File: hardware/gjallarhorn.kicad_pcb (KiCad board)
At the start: 2 copper layers, 18 parts, among them J1 Conn_01x02, J2 Conn_02x03_Counter_Clockwise, J3 Conn_01x02, J4 Conn_01x03, Q1 Q_NMOS_GDS, SW1 SW_Push, U1 ATTINY2313-20PU, U2 BOOST_REGULATOR, U3 AP1117-33, U4 HC-05_breakout

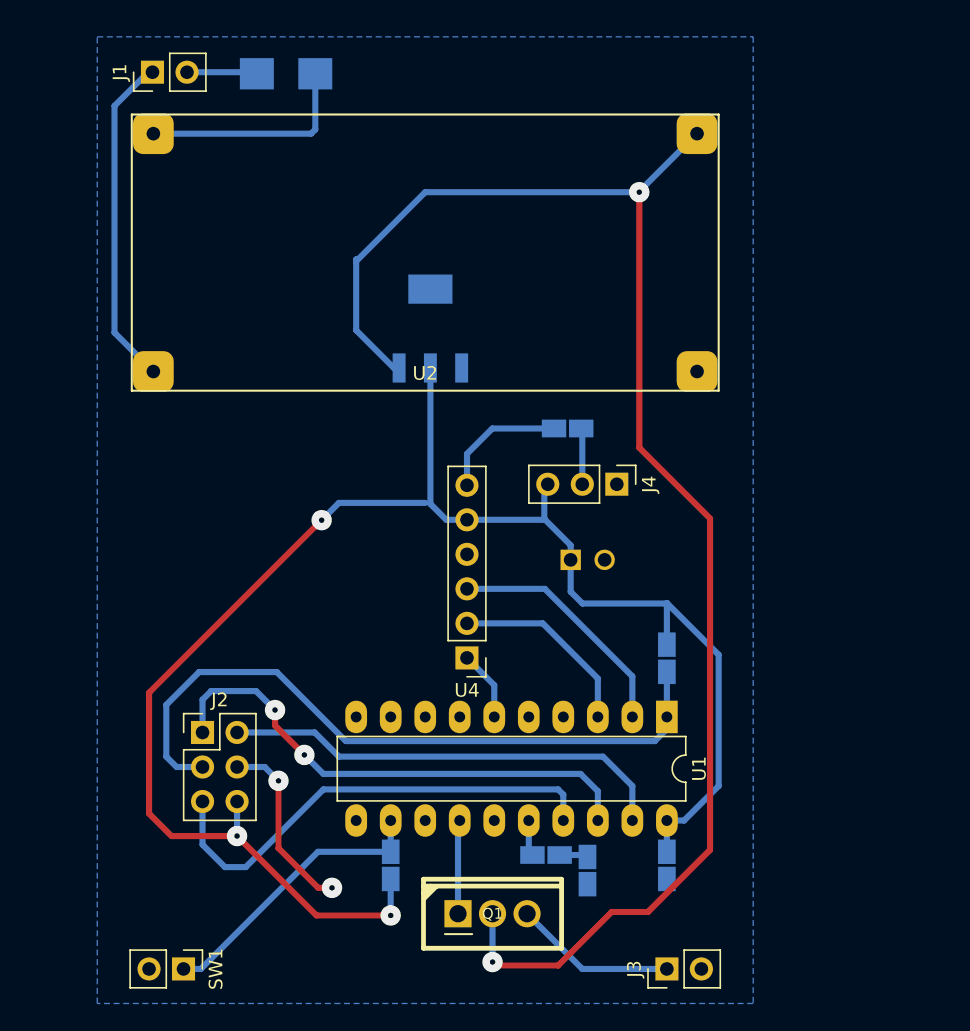
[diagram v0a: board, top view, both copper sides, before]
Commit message: It would be better if I could fit this in a 60x60 square; let's try (in progress).
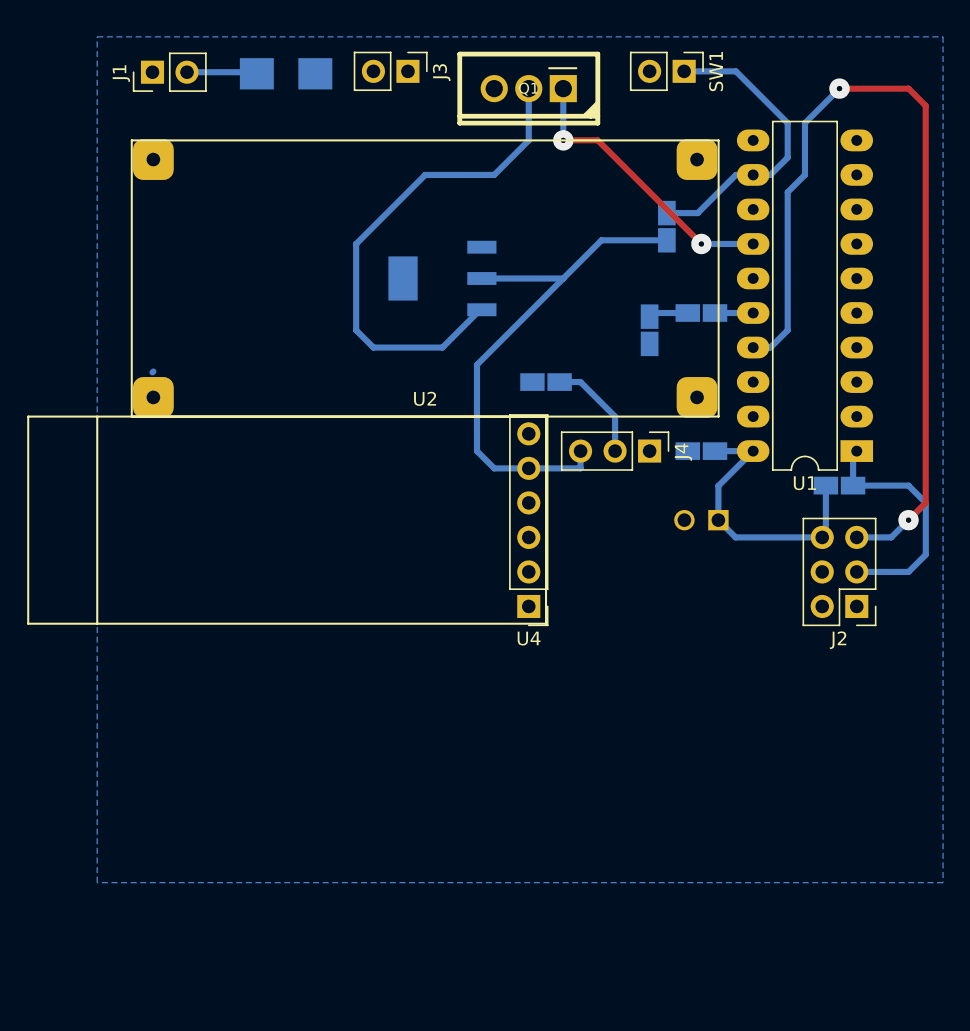
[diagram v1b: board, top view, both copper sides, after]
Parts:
- moved SW1 75.6 mm to (167.6, 38.1)
- moved J3 68.7 mm to (147.3, 38.1), turned to 270 degrees
- moved Q1 60.8 mm to (156.2, 39.4), turned to 180 degrees
- moved R3 51.2 mm to (166.4, 49.5)
- moved J2 49.0 mm to (180.3, 77.5), turned to 180 degrees
- moved R2 41.5 mm to (168.9, 55.9), turned to 180 degrees
- moved D1 40.0 mm to (165.1, 57.1)
- moved C1 30.6 mm to (168.9, 66.0), turned to 0 degrees
- moved U1 24.0 mm to (180.3, 66.0), turned to 180 degrees
- moved R1 18.0 mm to (179.1, 68.6), turned to 180 degrees
- moved C2 8.86 mm to (168.9, 71.1), turned to 270 degrees
- moved U4 5.92 mm to (156.2, 77.5)
- moved U3 3.79 mm to (149.9, 53.3), turned to 270 degrees
- moved R4 3.77 mm to (157.5, 61.0)
- moved J4 3.43 mm to (165.1, 66.0)
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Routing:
- net +12V: track 112.5 -> 36.9 mm, vias 2 -> 0
- net +3V3: track 121.5 -> 60.6 mm, vias 3 -> 0
- net Net-(J2-Pad1): track 37.6 -> 0.00 mm, vias 2 -> 0
- net Net-(J2-Pad3): track 51.3 -> 17.9 mm
- net Net-(J2-Pad2): track 33.3 -> 0.00 mm
- net Net-(J2-Pad5): track 34.8 -> 64.6 mm, vias 0 -> 2
- net Net-(J1-Pad1): track 24.6 -> 0.41 mm
- net Net-(U1-Pad2): track 17.8 -> 0.00 mm
- net Net-(D2-Pad1): track 16.1 -> 0.00 mm
- net Net-(U1-Pad3): track 14.1 -> 0.00 mm
- net GND: track 13.6 -> 0.00 mm, vias 2 -> 0
- net Net-(Q1-Pad1): track 7.80 -> 20.9 mm, vias 0 -> 2
- net Net-(J3-Pad1): track 12.0 -> 0.00 mm
- net Net-(R4-Pad2): track 9.49 -> 0.00 mm
- net Net-(U1-Pad6): track 5.17 -> 0.00 mm
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
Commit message: Moving everything everywhere.
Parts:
- removed J4: Conn_01x03, KiCad/Pin_Headers.pretty:Pin_Header_Straight_1x03_Pitch2.54mm
- added R5: 10k, coddingtonbear/coddingtonbear.pretty:0805_Milling, B.Cu at (139.7, 69.2)
- added R6: 6.8k, coddingtonbear/coddingtonbear.pretty:0805_Milling, B.Cu at (129.5, 76.8)
- added R7: 10k, coddingtonbear/coddingtonbear.pretty:0805_Milling, B.Cu at (129.5, 74.3)
- J1: value Conn_01x02 -> VIN
- J2: value Conn_02x03_Counter_Clockwise -> PROG
- J3: value Conn_01x02 -> HORN
- R4: value 10k -> 6.8k
- U3: value AP1117-33 -> AP1117-5.0
- moved J3 35.7 mm to (182.9, 40.6), turned to 180 degrees
- moved R2 26.1 mm to (157.5, 79.4)
- moved D1 25.3 mm to (153.0, 79.4), turned to 0 degrees
- moved Q1 21.7 mm to (176.5, 47.0), turned to 0 degrees
- moved SW1 21.1 mm to (182.9, 52.7), turned to 0 degrees
- moved R4 20.8 mm to (139.7, 71.8)
- moved U4 19.1 mm to (141.0, 66.0), turned to 270 degrees
- moved R3 14.1 mm to (179.7, 54.0)
- moved U1 11.7 mm to (168.9, 68.6), turned to 270 degrees
- moved C2 11.3 mm to (175.9, 62.2), turned to 180 degrees
- moved R1 7.10 mm to (172.1, 67.3), turned to 90 degrees
- moved U3 6.20 mm to (154.9, 49.8), turned to 90 degrees
- moved C1 4.96 mm to (172.1, 62.2), turned to 270 degrees
- moved J2 3.42 mm to (181.6, 74.3)
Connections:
- net Net-(J2-Pad1) renamed MISO
- net Net-(U1-Pad2) renamed RX
- C1 pad 2: +3V3 -> +5V
- C2 pad 1: +3V3 -> +5V
- J1 pad 1: Net-(J1-Pad1) -> GND
- J2 pad 2: Net-(J2-Pad2) -> +5V
- J2 pad 3: Net-(J2-Pad3) -> SCK
- J2 pad 4: GND -> MOSI
- J2 pad 5: Net-(J2-Pad5) -> RESET
- J2 pad 6: +3V3 -> GND
- Q1 pad 1: Net-(Q1-Pad1) -> HORN
- R1 pad 1: Net-(J2-Pad3) -> RESET
- R1 pad 2: +3V3 -> +5V
- R3 pad 2: +3V3 -> +5V
- R4 pad 1: Net-(J4-Pad2) -> TX
- U1 pad 1: Net-(J2-Pad3) -> RESET
- U1 pad 11: Net-(U1-Pad11) -> BT_ENABLE
- U1 pad 12: Net-(R3-Pad1) -> Net-(U1-Pad12)
- U1 pad 14: Net-(Q1-Pad1) -> Net-(U1-Pad14)
- U1 pad 17: Net-(J2-Pad5) -> MOSI
- U1 pad 19: Net-(J2-Pad2) -> SCK
- U1 pad 20: +3V3 -> +5V
- U1 pad 3: Net-(U1-Pad3) -> TX
- U1 pad 6: Net-(U1-Pad6) -> Net-(R3-Pad1)
- U1 pad 7: Net-(U1-Pad7) -> HORN
- U1 pad 9: Net-(U1-Pad9) -> BT_STATE
- U2 pad 2: Net-(J1-Pad1) -> GND
- U3 pad 2: +3V3 -> +5V
- U4 pad 1: Net-(U1-Pad6) -> BT_STATE
- U4 pad 2: Net-(U1-Pad3) -> Net-(R4-Pad2)
- U4 pad 5: +3V3 -> +5V
- U4 pad 6: Net-(R4-Pad2) -> Net-(R6-Pad2)
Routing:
- net +5V: track 0.00 -> 104.6 mm, vias 0 -> 5
- net Net-(J2-Pad5): track 64.6 -> 0.00 mm, vias 2 -> 0
- net +3V3: track 60.6 -> 0.00 mm
- net RX: track 0.00 -> 38.5 mm, vias 0 -> 2
- net HORN: track 0.00 -> 31.1 mm
- net SCK: track 0.00 -> 27.6 mm
- net TX: track 0.00 -> 26.9 mm
- net MISO: track 0.00 -> 25.4 mm
- net GND: track 0.00 -> 23.1 mm, vias 0 -> 2
- net MOSI: track 0.00 -> 21.1 mm
- net Net-(Q1-Pad1): track 20.9 -> 0.00 mm, vias 2 -> 0
- net Net-(J2-Pad3): track 17.9 -> 0.00 mm
- net RESET: track 0.00 -> 17.2 mm, vias 0 -> 2
- net Net-(D2-Pad1): track 0.00 -> 16.5 mm
- net BT_ENABLE: track 0.00 -> 15.8 mm
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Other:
- board text added: "- +"

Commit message: Final version.
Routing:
- net GND: track 23.1 -> 28.1 mm, vias 2 -> 4
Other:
- board outline added: 62.2 x 47 mm

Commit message: Let's...make a couple more changes.
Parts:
- removed SW1: SW_Push, KiCad/Pin_Headers.pretty:Pin_Header_Straight_1x02_Pitch2.54mm
- added J4: BUTTON-, coddingtonbear/coddingtonbear.pretty:TAB, F.Cu at (179.1, 52.1)
- added J5: BUTTON+, coddingtonbear/coddingtonbear.pretty:TAB, F.Cu at (179.1, 57.1)
- added J6: HORN+, coddingtonbear/coddingtonbear.pretty:TAB, F.Cu at (179.1, 38.1)
- added J7: HORN-, coddingtonbear/coddingtonbear.pretty:TAB, F.Cu at (167.6, 38.1)
- J1: value VIN -> VCC; footprint KiCad/Pin_Headers.pretty:Pin_Header_Straight_1x02_Pitch2.54mm -> coddingtonbear/coddingtonbear.pretty:TAB
- J3: value HORN -> GND; footprint KiCad/Pin_Headers.pretty:Pin_Header_Straight_1x02_Pitch2.54mm -> coddingtonbear/coddingtonbear.pretty:TAB
- moved J3 52.1 mm to (130.8, 38.1)
- moved R3 19.9 mm to (160.7, 59.7), turned to 0 degrees
- moved D2 16.6 mm to (154.9, 38.1)
- moved J1 15.0 mm to (143.5, 38.1), turned to 180 degrees
- moved U3 7.28 mm to (148.6, 53.3)
- moved Q1 2.84 mm to (179.1, 45.7)
- moved C2 1.42 mm to (176.5, 63.5), turned to 0 degrees
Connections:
- J1 pad 1: GND -> Net-(D2-Pad2)
- J3 pad 1: Net-(J3-Pad1) -> GND
- Q1 pad 3: Net-(J3-Pad1) -> Net-(J6-Pad1)
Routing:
- net Net-(D2-Pad1): track 16.5 -> 32.9 mm
- net Net-(J6-Pad1): track 0.00 -> 12.6 mm
- net +12V: track 31.2 -> 40.9 mm
- net Net-(J3-Pad1): track 8.67 -> 0.00 mm
- net Net-(D2-Pad2): track 5.19 -> 11.8 mm
- net HORN: track 31.1 -> 36.0 mm
- net GND: track 28.1 -> 31.4 mm
- net Net-(J4-Pad1): track 34.4 -> 36.8 mm
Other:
- board text added: "+"
- board text added: "-"
- board text added: "ACT"
- board text added: "HORN"
- board text added: "POWER"
- board text removed: "- +"

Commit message: I guess I can make another?
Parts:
- moved J2 2.93 mm to (181.4, 77.2)
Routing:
- net GND: track 31.4 -> 41.2 mm, vias 4 -> 6
- net MISO: track 25.4 -> 23.5 mm
- net +5V: track 105.1 -> 106.8 mm, vias 5 -> 6
- net RESET: track 17.2 -> 16.0 mm, vias 2 -> 0
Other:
- net class Default: via_dia 1.5 -> 2
- board text added: "@coddingtonbear 4 October 2017 “gjallarhorn”"
- board text added: "◤"
